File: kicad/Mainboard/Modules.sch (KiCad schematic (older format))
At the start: 2 parts

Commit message: Add files via upload
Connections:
- net +3V3: now also U?.12 (GPIO0); no longer U?.1 (REST)
- new net WIFI_RST: U?.1 (REST)
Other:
- moved on the sheet: 10u, U?
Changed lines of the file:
@@
 encoding utf-8
 Sheet 8 8
-Title ""
-Date ""
+Title "Modules"
+Date "2020-01-20"
 Rev ""
 Comp ""
@@
 Comment2 ""
 Comment3 ""
-Comment4 ""
+Comment4 "TR-9 Open Source Digital Radio"
 $EndDescr
 $Comp
 L ESP8266:ESP-12F U?
 U 1 1 5E25657C
-P 3500 3750
-F 0 "U?" H 3500 4515 50  0000 C CNN
-F 1 "ESP-12F" H 3500 4424 50  0000 C CNN
-F 2 "" H 3500 3750 50  0001 C CNN
-F 3 "" H 3500 3750 50  0001 C CNN
-	1    3500 3750
+P 5750 3700
+F 0 "U?" H 5750 4465 50  0000 C CNN
+F 1 "ESP-12F" H 5750 4374 50  0000 C CNN
+F 2 "" H 5750 3700 50  0001 C CNN
+F 3 "" H 5750 3700 50  0001 C CNN
+	1    5750 3700
 	1    0    0    -1
 $EndComp
@@
 L power:+3.3V #PWR?
 U 1 1 5E2571F1
-P 2450 4150
-F 0 "#PWR?" H 2450 4000 50  0001 C CNN
-F 1 "+3.3V" V 2465 4278 50  0000 L CNN
-F 2 "" H 2450 4150 50  0001 C CNN
-F 3 "" H 2450 4150 50  0001 C CNN
-	1    2450 4150
+P 4700 4100
+F 0 "#PWR?" H 4700 3950 50  0001 C CNN
+F 1 "+3.3V" V 4715 4228 50  0000 L CNN
+F 2 "" H 4700 4100 50  0001 C CNN
+F 3 "" H 4700 4100 50  0001 C CNN
+	1    4700 4100
 	0    -1   -1   0
 $EndComp
 Wire Wire Line
-	2450 4150 2500 4150
+	4700 4100 4750 4100
 $Comp
 L Device:C 10u
 U 1 1 5E258338
-P 2500 4400
-F 0 "10u" H 2615 4446 50  0000 L CNN
-F 1 "C" H 2615 4355 50  0000 L CNN
-F 2 "" H 2538 4250 50  0001 C CNN
-F 3 "~" H 2500 4400 50  0001 C CNN
-	1    2500 4400
+P 4750 4350
+F 0 "10u" H 4865 4396 50  0000 L CNN
+F 1 "C" H 4865 4305 50  0000 L CNN
+F 2 "" H 4788 4200 50  0001 C CNN
+F 3 "~" H 4750 4350 50  0001 C CNN
+	1    4750 4350
 	1    0    0    -1
 $EndComp
@@
 L power:GND #PWR?
 U 1 1 5E259225
-P 2500 4800
-F 0 "#PWR?" H 2500 4550 50  0001 C CNN
-F 1 "GND" H 2505 4627 50  0000 C CNN
-F 2 "" H 2500 4800 50  0001 C CNN
-F 3 "" H 2500 4800 50  0001 C CNN
-	1    2500 4800
+P 4750 4550
+F 0 "#PWR?" H 4750 4300 50  0001 C CNN
+F 1 "GND" H 4755 4377 50  0000 C CNN
+F 2 "" H 4750 4550 50  0001 C CNN
+F 3 "" H 4750 4550 50  0001 C CNN
+	1    4750 4550
 	1    0    0    -1
 $EndComp
 Wire Wire Line
-	2500 4550 2500 4800
-Wire Wire Line
-	2500 4250 2500 4150
-Connection ~ 2500 4150
+	4750 4200 4750 4100
+Connection ~ 4750 4100
 $Comp
 L power:GND #PWR?
 U 1 1 5E259705
-P 4500 4800
-F 0 "#PWR?" H 4500 4550 50  0001 C CNN
-F 1 "GND" H 4505 4627 50  0000 C CNN
-F 2 "" H 4500 4800 50  0001 C CNN
-F 3 "" H 4500 4800 50  0001 C CNN
-	1    4500 4800
+P 6750 4550
+F 0 "#PWR?" H 6750 4300 50  0001 C CNN
+F 1 "GND" H 6755 4377 50  0000 C CNN
+F 2 "" H 6750 4550 50  0001 C CNN
+F 3 "" H 6750 4550 50  0001 C CNN
+	1    6750 4550
 	1    0    0    -1
 $EndComp
 Wire Wire Line
-	2500 4150 2600 4150
+	4750 4100 4850 4100
+Wire Wire Line
+	4700 3400 4850 3400
+Wire Wire Line
+	4850 3600 4700 3600
+Wire Wire Line
+	6650 4100 6750 4100
+Text GLabel 4700 3600 0    50   Input ~ 10
+WIFI_EN
+Text GLabel 6750 3500 2    50   Input ~ 10
+USART3_TX
+Text GLabel 6750 3400 2    50   Input ~ 10
+USART3_RX
 $Comp
 L power:+3.3V #PWR?
-U 1 1 5E25E60B
-P 2450 3450
-F 0 "#PWR?" H 2450 3300 50  0001 C CNN
-F 1 "+3.3V" V 2465 3578 50  0000 L CNN
-F 2 "" H 2450 3450 50  0001 C CNN
-F 3 "" H 2450 3450 50  0001 C CNN
-	1    2450 3450
-	0    -1   -1   0
+U 1 1 5E25DB0A
+P 6750 3800
+F 0 "#PWR?" H 6750 3650 50  0001 C CNN
+F 1 "+3.3V" V 6765 3928 50  0000 L CNN
+F 2 "" H 6750 3800 50  0001 C CNN
+F 3 "" H 6750 3800 50  0001 C CNN
+	1    6750 3800
+	0    1    1    0
 $EndComp
 Wire Wire Line
-	2450 3450 2600 3450
+	6750 3800 6650 3800
+Text GLabel 4700 3400 0    50   Input ~ 10
+WIFI_RST
 Wire Wire Line
-	4500 4150 4500 4800
+	4750 4500 4750 4550
 Wire Wire Line
-	2600 3650 2450 3650
+	6750 4100 6750 4550
 Wire Wire Line
-	4400 3450 4650 3450
+	6650 3400 6750 3400
 Wire Wire Line
-	4400 3550 4650 3550
-Wire Wire Line
-	4400 4150 4500 4150
-Text GLabel 2450 3650 0    50   Input ~ 10
-WIFI_EN
-Text GLabel 4650 3550 2    50   Input ~ 10
-USART3_TX
-Text GLabel 4650 3450 2    50   Input ~ 10
-USART3_RX
+	6650 3500 6750 3500
 $EndSCHEMATC

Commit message: Annotated parts, again.
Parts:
- gave numbers to parts that had none: 1
- renumbered 10u to 10u1
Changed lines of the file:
@@
 EESchema Schematic File Version 4
-LIBS:Mainboard-cache
 EELAYER 30 0
 EELAYER END
@@
 $EndDescr
 $Comp
-L ESP8266:ESP-12F U?
+L ESP8266:ESP-12F U12
 U 1 1 5E25657C
 P 5750 3700
-F 0 "U?" H 5750 4465 50  0000 C CNN
+F 0 "U12" H 5750 4465 50  0000 C CNN
 F 1 "ESP-12F" H 5750 4374 50  0000 C CNN
 F 2 "" H 5750 3700 50  0001 C CNN
@@
 $EndComp
 $Comp
-L power:+3.3V #PWR?
+L power:+3.3V #PWR0171
 U 1 1 5E2571F1
 P 4700 4100
-F 0 "#PWR?" H 4700 3950 50  0001 C CNN
+F 0 "#PWR0171" H 4700 3950 50  0001 C CNN
 F 1 "+3.3V" V 4715 4228 50  0000 L CNN
 F 2 "" H 4700 4100 50  0001 C CNN
@@
 	4700 4100 4750 4100
 $Comp
-L Device:C 10u
+L Device:C 10u1
 U 1 1 5E258338
 P 4750 4350
-F 0 "10u" H 4865 4396 50  0000 L CNN
+F 0 "10u1" H 4865 4396 50  0000 L CNN
 F 1 "C" H 4865 4305 50  0000 L CNN
 F 2 "" H 4788 4200 50  0001 C CNN
@@
 $EndComp
 $Comp
-L power:GND #PWR?
+L power:GND #PWR0172
 U 1 1 5E259225
 P 4750 4550
-F 0 "#PWR?" H 4750 4300 50  0001 C CNN
+F 0 "#PWR0172" H 4750 4300 50  0001 C CNN
 F 1 "GND" H 4755 4377 50  0000 C CNN
 F 2 "" H 4750 4550 50  0001 C CNN
@@
 Connection ~ 4750 4100
 $Comp
-L power:GND #PWR?
+L power:GND #PWR0174
 U 1 1 5E259705
 P 6750 4550
-F 0 "#PWR?" H 6750 4300 50  0001 C CNN
+F 0 "#PWR0174" H 6750 4300 50  0001 C CNN
 F 1 "GND" H 6755 4377 50  0000 C CNN
 F 2 "" H 6750 4550 50  0001 C CNN
@@
 USART3_RX
 $Comp
-L power:+3.3V #PWR?
+L power:+3.3V #PWR0173
 U 1 1 5E25DB0A
 P 6750 3800
-F 0 "#PWR?" H 6750 3650 50  0001 C CNN
+F 0 "#PWR0173" H 6750 3650 50  0001 C CNN
 F 1 "+3.3V" V 6765 3928 50  0000 L CNN
 F 2 "" H 6750 3800 50  0001 C CNN

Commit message: Started assigning footprints
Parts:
- C94: renamed from 10u1; value C -> 10u1; footprint (none) -> Capacitor_SMD:C_0603_1608Metric; symbol Device:C -> Mainboard-rescue:C-Device
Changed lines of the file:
@@
 	4700 4100 4750 4100
 $Comp
-L Device:C 10u1
+L Mainboard-rescue:C-Device C94
 U 1 1 5E258338
 P 4750 4350
-F 0 "10u1" H 4865 4396 50  0000 L CNN
-F 1 "C" H 4865 4305 50  0000 L CNN
-F 2 "" H 4788 4200 50  0001 C CNN
+F 0 "C94" H 4865 4396 50  0000 L CNN
+F 1 "10u1" H 4865 4305 50  0000 L CNN
+F 2 "Capacitor_SMD:C_0603_1608Metric" H 4788 4200 50  0001 C CNN
 F 3 "~" H 4750 4350 50  0001 C CNN
 	1    4750 4350

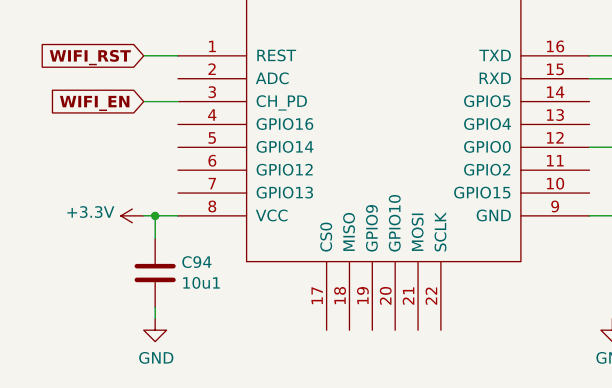
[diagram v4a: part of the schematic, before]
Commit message: Add files via upload
C94 -> 10uF
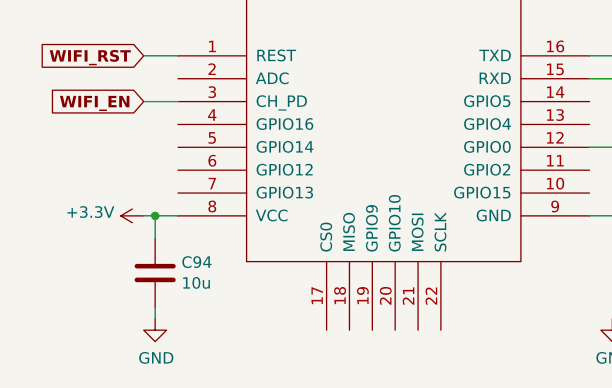
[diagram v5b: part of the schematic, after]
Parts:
- C94: value 10u1 -> 10u
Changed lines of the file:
@@
 P 4750 4350
 F 0 "C94" H 4865 4396 50  0000 L CNN
-F 1 "10u1" H 4865 4305 50  0000 L CNN
+F 1 "10u" H 4865 4305 50  0000 L CNN
 F 2 "Capacitor_SMD:C_0603_1608Metric" H 4788 4200 50  0001 C CNN
 F 3 "~" H 4750 4350 50  0001 C CNN

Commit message: Add files via upload
assigned some more footprints
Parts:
- U12: footprint (none) -> RF_Module:ESP-12E
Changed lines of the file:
@@
 F 0 "U12" H 5750 4465 50  0000 C CNN
 F 1 "ESP-12F" H 5750 4374 50  0000 C CNN
-F 2 "" H 5750 3700 50  0001 C CNN
+F 2 "RF_Module:ESP-12E" H 5750 3700 50  0001 C CNN
 F 3 "" H 5750 3700 50  0001 C CNN
 	1    5750 3700

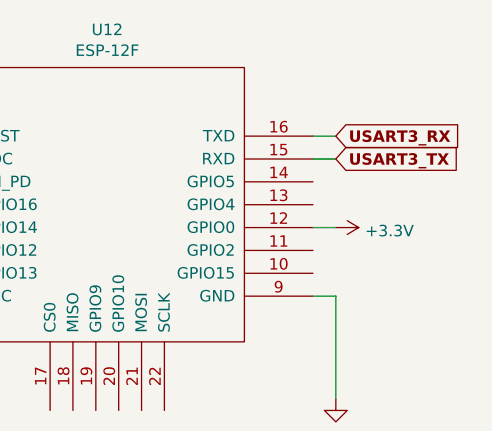
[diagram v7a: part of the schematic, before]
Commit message: Added thermal vias to BGA6589 footprint Corrected USART to UART
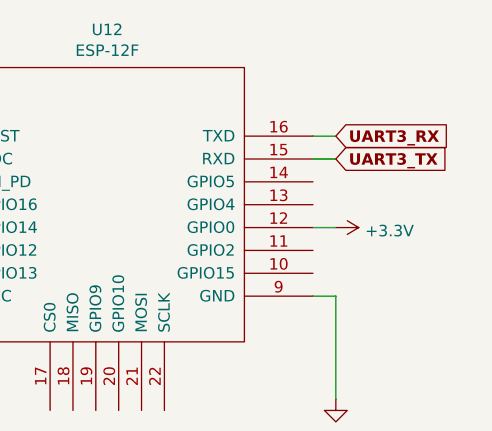
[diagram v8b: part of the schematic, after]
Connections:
- net USART3_RX renamed UART3_RX
- net USART3_TX renamed UART3_TX
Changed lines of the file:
@@
 WIFI_EN
 Text GLabel 6750 3500 2    50   Input ~ 10
-USART3_TX
+UART3_TX
 Text GLabel 6750 3400 2    50   Input ~ 10
-USART3_RX
+UART3_RX
 $Comp
 L power:+3.3V #PWR0173
